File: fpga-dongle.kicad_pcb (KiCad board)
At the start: 2 copper layers, 85.8 x 137 mm, 103 parts, among them P1 USB_PWR, P2 PGM, P3 right, P4 left, P5 CONN_01X40, P6 CONN_01X40, P7 DBG_SWD, P8 USB_PWR, Q1 BC857, SW1 T1107A(6x3,8x2,5MM), U1 W25Q16BVSSIG(SOIC-8_208mil), U2 sc189(Z) 3.3v, U3 sc189(C) 1.2v, U4 iCE40-HX4K-TQ144, U5 AS4C16M16S, U6 LPC11U35FBD48, X1 12MHz

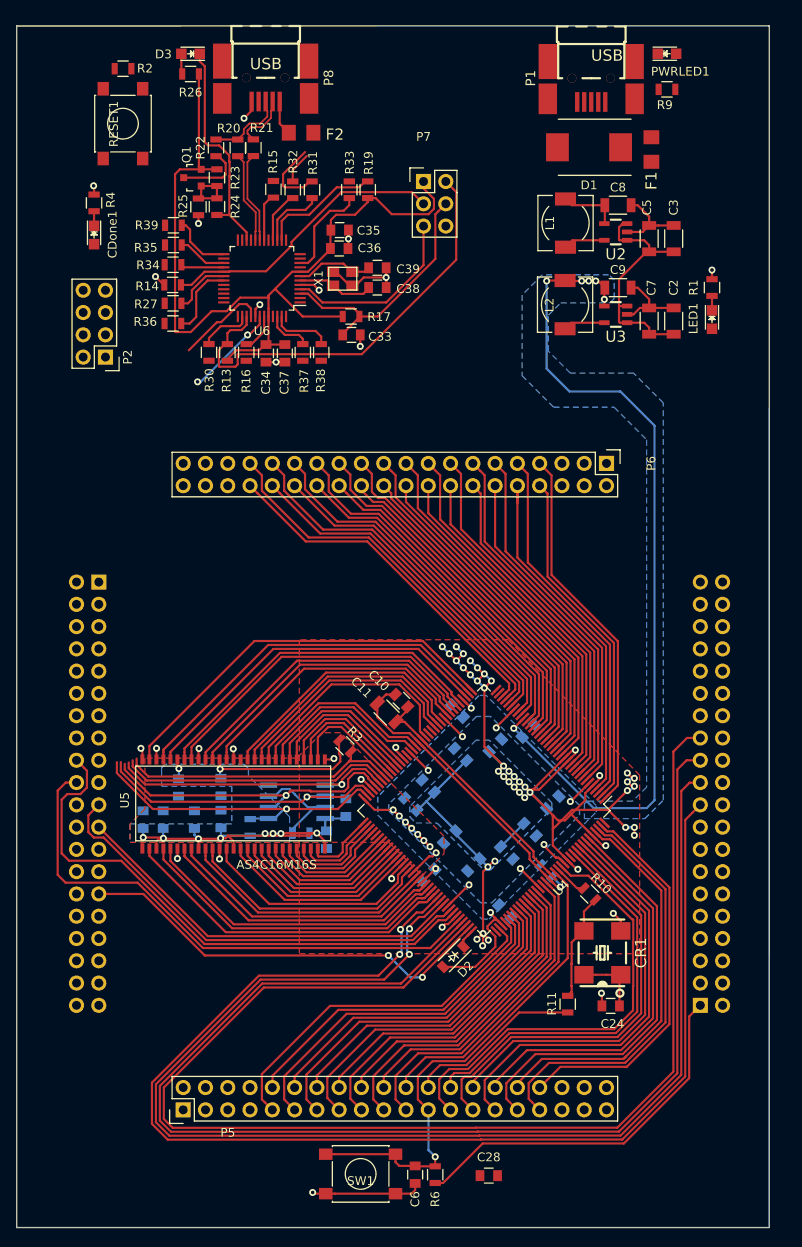
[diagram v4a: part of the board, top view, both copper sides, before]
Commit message: More route (PWR net connectors TODO)
Signed-off-by: Martin Ribelotta <martinribelotta@gmail.com>
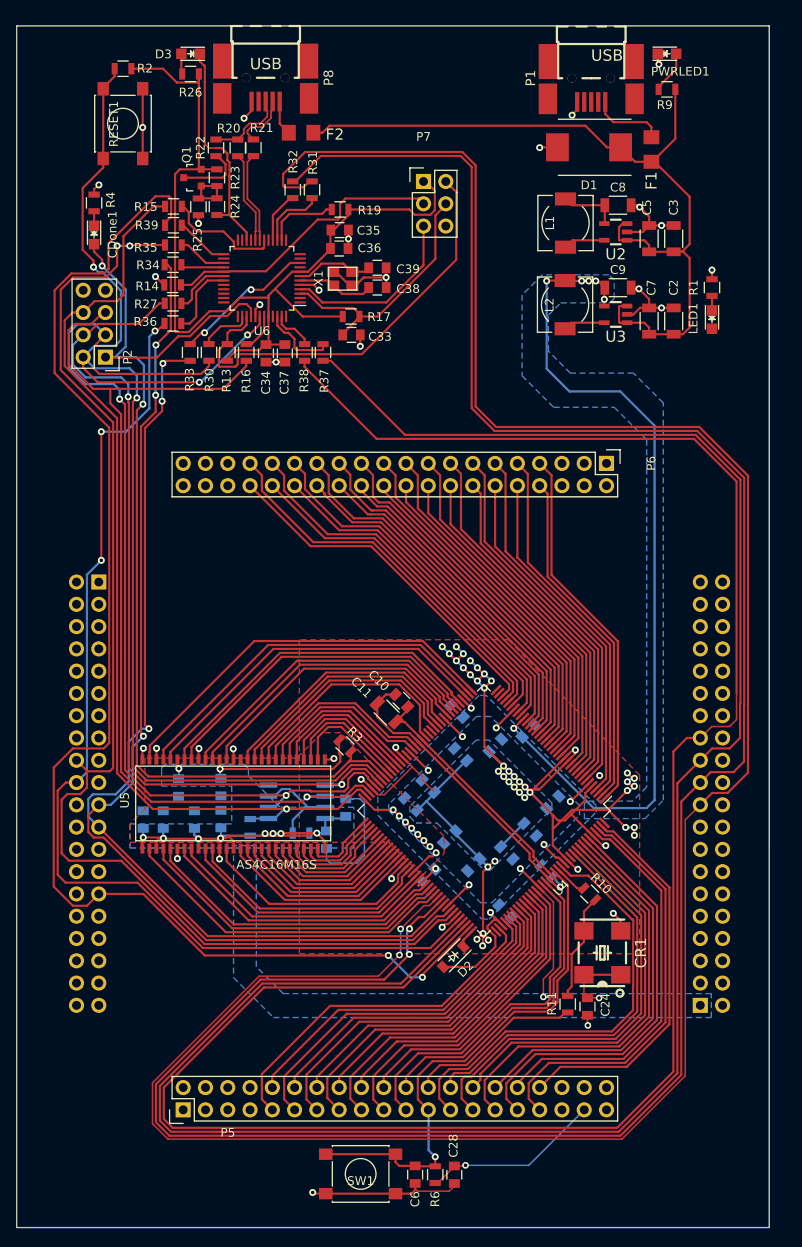
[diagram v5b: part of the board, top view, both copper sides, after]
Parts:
- moved R33 26.0 mm to (35.0, 54.9), turned to 270 degrees
- moved R15 11.6 mm to (33.1, 38.2), turned to 180 degrees
- moved C28 3.93 mm to (65.2, 148.6), turned to 270 degrees
- moved R19 3.87 mm to (52.1, 38.5), turned to 0 degrees
- moved C24 2.65 mm to (80.3, 129.4), turned to 270 degrees
- moved R37 2.30 mm to (50.2, 54.9)
- moved R38 1.90 mm to (48.1, 54.9)
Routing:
- net /I2C_SDA: track 152.7 -> 274.9 mm
- net /I2C_SCL: track 149.5 -> 267.5 mm
- net /iCE40-CRESET: track 41.9 -> 147.5 mm, vias 2 -> 4
- net /GPIO0: track 48.7 -> 153.4 mm
- net /TxD: track 147.0 -> 234.5 mm
- net /RxD: track 146.2 -> 233.5 mm
- net /iCE40-SDI: track 36.2 -> 113.7 mm, vias 1 -> 2
- net /SPI_MISO: track 63.6 -> 139.1 mm, vias 0 -> 2
- net /iCE40-SCK: track 34.1 -> 109.1 mm
- net /iCE40-CDONE: track 42.6 -> 117.3 mm, vias 0 -> 2
- net /iCE40-SS_B: track 37.2 -> 110.8 mm
- net +5V: track 28.4 -> 96.0 mm
- net /SPI_MOSI: track 51.4 -> 117.9 mm, vias 0 -> 3
- net /iCE40-SDO: track 33.6 -> 98.6 mm, vias 1 -> 2
- net /SPI_CS: track 46.0 -> 108.5 mm, vias 0 -> 3
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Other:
- net class Default: clearance 0.2 -> 0.1778; trace_width 0.25 -> 0.1778; via_dia 0.8 -> 0.762; via_drill 0.4 -> 0.4064
- rule trace_clearance: 0.2 -> 0.1778
- rule trace_min: 0.2 -> 0.1778
- rule via_min_drill: 0.3 -> 0.4064
- rule via_min_size: 0.4 -> 0.7112

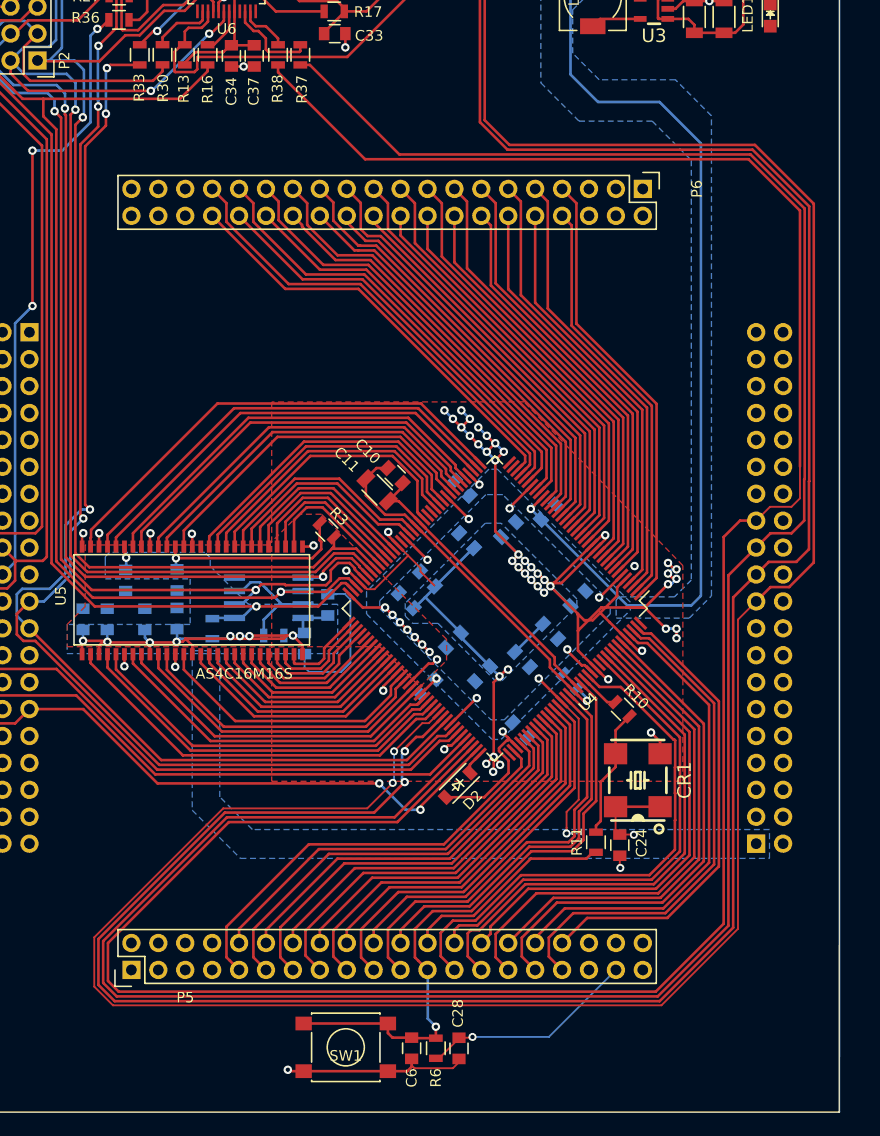
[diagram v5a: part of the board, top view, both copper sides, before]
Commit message: First DRC pass. Remain unconenct some 3v3 and 5v
Signed-off-by: Martin Ribelotta <martinribelotta@gmail.com>
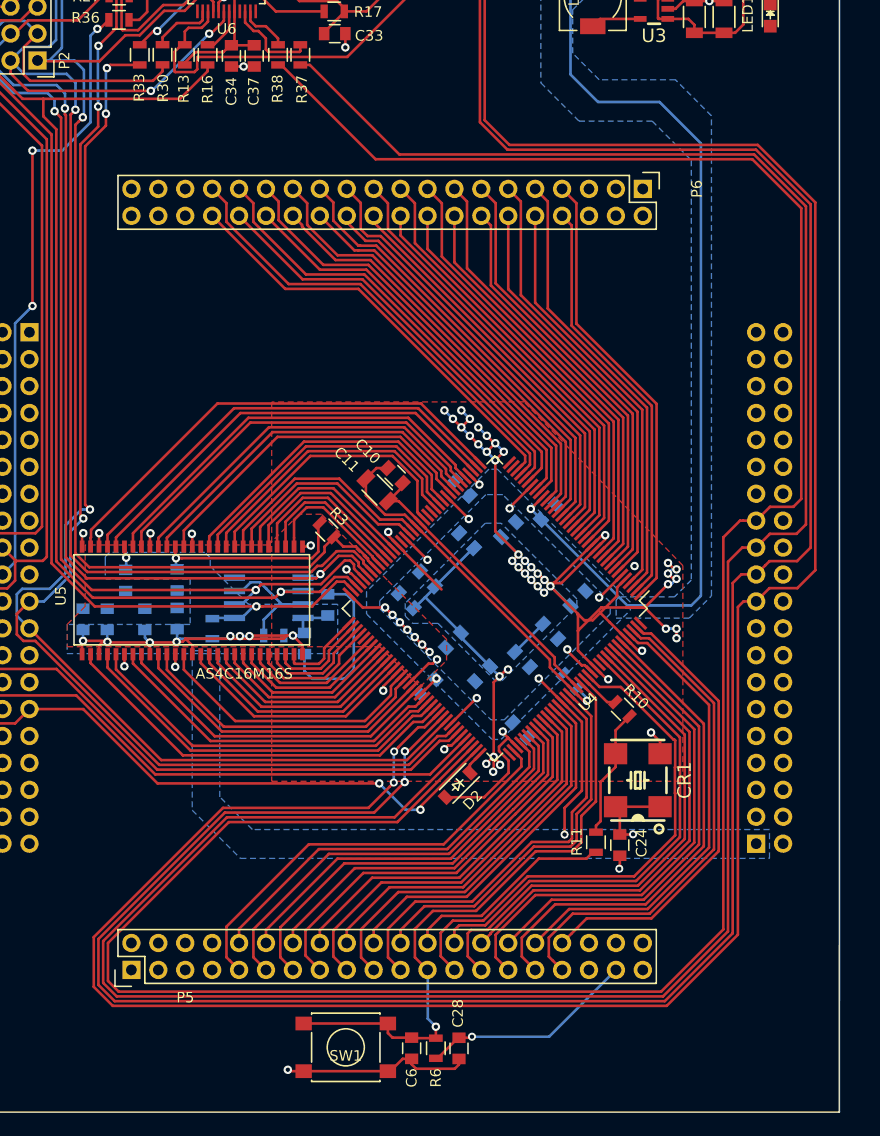
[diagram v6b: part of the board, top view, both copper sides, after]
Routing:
- net GND: track 258.8 -> 254.5 mm
- net /I2C_SDA: track 274.9 -> 276.9 mm
- net /RxD: track 233.5 -> 235.2 mm
- net +3V3: track 263.9 -> 262.6 mm
- net /FPGA_IO_BANK1_17: track 45.6 -> 44.5 mm
- net /FPGA_IO_BANK1_21: track 45.0 -> 43.9 mm
- net /I2C_SCL: track 267.5 -> 268.6 mm
- net /FPGA_IO_BANK1_23: track 44.0 -> 43.2 mm
- net /FPGA_IO_BANK1_22: track 47.7 -> 46.9 mm
- net /FPGA_IO_BANK1_18: track 48.4 -> 47.5 mm
- net /FPGA_IO_BANK1_20: track 47.6 -> 46.8 mm
- net /FPGA_IO_BANK1_19: track 44.6 -> 43.8 mm
- net /FPGA_IO_BANK1_16: track 49.2 -> 48.4 mm
- net /FPGA_IO_BANK1_15: track 46.6 -> 45.8 mm
- net /FPGA_IO_BANK1_14: track 50.5 -> 49.7 mm
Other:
- net class Default: clearance 0.1778 -> 0.1905; trace_width 0.1778 -> 0.25
- rule trace_clearance: 0.1778 -> 0.1905
- rule trace_min: 0.1778 -> 0.2032

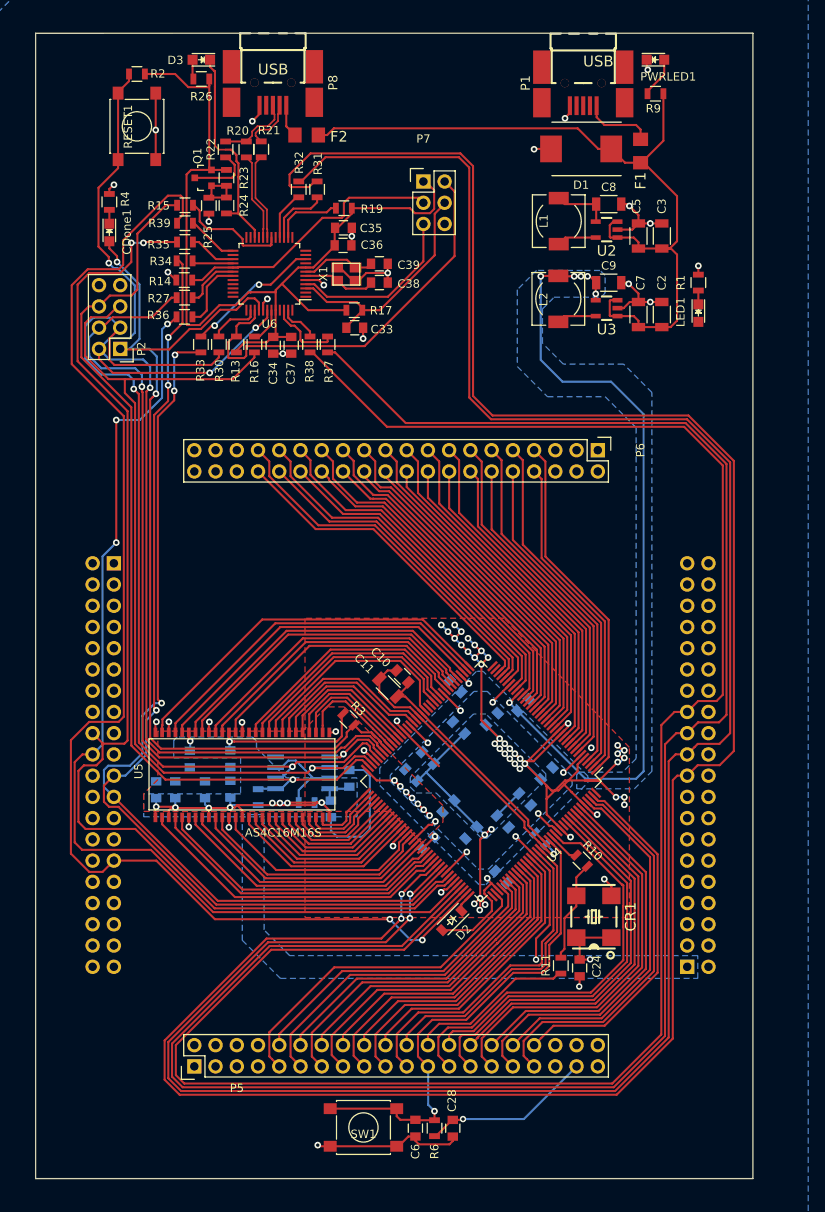
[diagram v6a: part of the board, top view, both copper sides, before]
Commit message: Fix CIAA connector side error, power net route
Signed-off-by: Martin Ribelotta <martinribelotta@gmail.com>
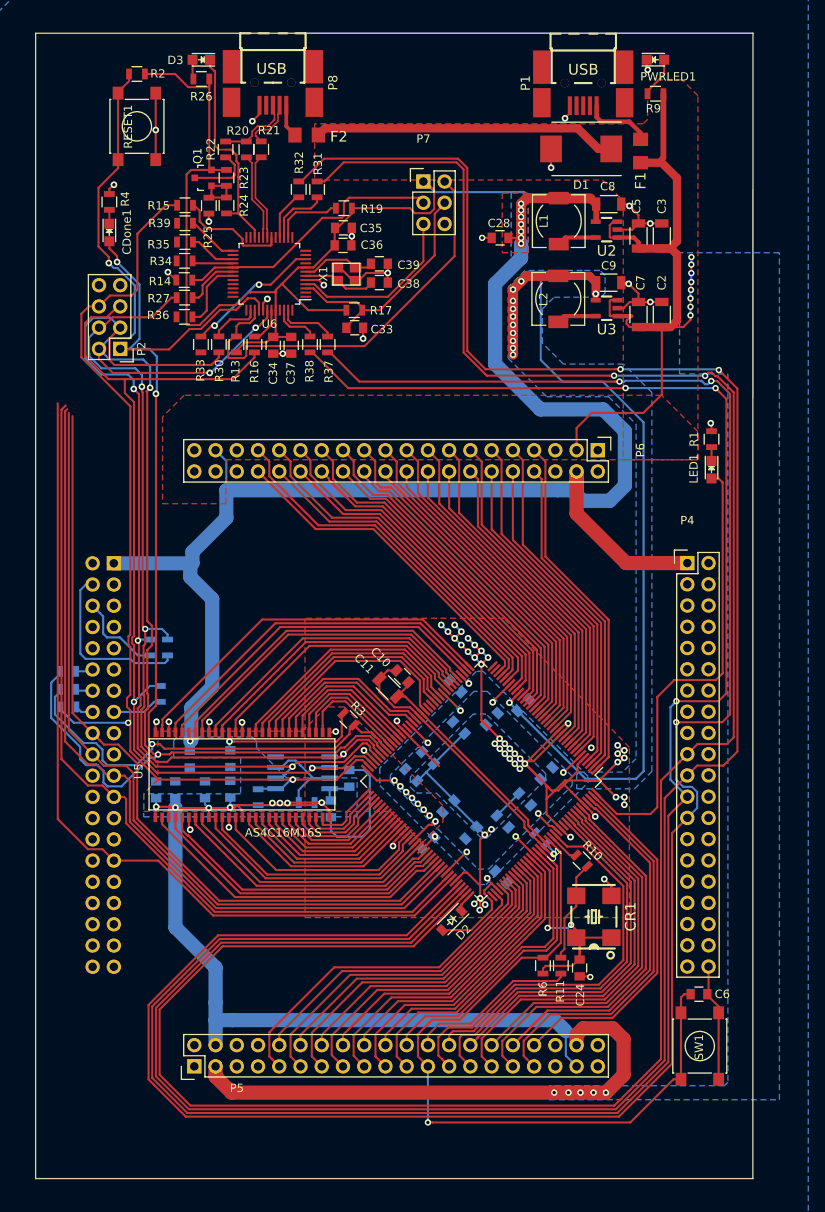
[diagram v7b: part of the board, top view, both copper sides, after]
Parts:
- added R18: 100R, Resistors_SMD:R_0805, B.Cu at (28.9, 91.1)
- added R28: 100R, Resistors_SMD:R_0805, B.Cu at (19.2, 98.2)
- added R29: 100R, Resistors_SMD:R_0805, B.Cu at (30.2, 96.7)
- added R40: 100R, Resistors_SMD:R_0805, B.Cu at (19.1, 96.1)
- added R41: 100R, Resistors_SMD:R_0805, B.Cu at (19.1, 94.0)
- added R7: 100R, Resistors_SMD:R_0805, B.Cu at (31.1, 91.1)
- P4: moved to F.Cu
- moved C28 106.7 mm to (70.8, 42.1), turned to 180 degrees
- moved P4 48.3 mm to (93.2, 81.0)
- moved SW1 41.4 mm to (94.7, 138.8), turned to 270 degrees
- moved C6 37.5 mm to (94.6, 132.6), turned to 180 degrees
- moved R6 23.4 mm to (76.0, 129.2)
- moved LED1 18.8 mm to (96.1, 69.8)
- moved R1 18.8 mm to (96.1, 66.2)
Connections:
- P3 pad 12: (no net) -> /AUX_CRESET
- P3 pad 14: (no net) -> /AUX_CDONE
- P3 pad 15: (no net) -> /AUX_SPI_SCK
- P3 pad 16: (no net) -> /AUX_SPI_SSEL
- P3 pad 4: (no net) -> /AUX_SPI_MISO
- P3 pad 6: (no net) -> /AUX_SPI_MOSI
- P4 pad 10: GNDA -> GND
- P4 pad 12: GNDA -> GND
- P4 pad 14: GNDA -> GND
- P4 pad 16: GNDA -> GND
- P4 pad 18: GNDA -> GND
- P4 pad 8: GNDA -> GND
- R37 pad 1: /P_RxD -> /P_TxD
- R37 pad 2: /RxD -> /TxD
- R38 pad 1: /P_TxD -> /P_RxD
- R38 pad 2: /TxD -> /RxD
- U4 pad 101: /SPI_MOSI -> /SPI_CS
- U4 pad 102: /SPI_MISO -> /GPIO0
- U4 pad 104: /SPI_CLK -> /TxD
- U4 pad 106: /TxD -> /I2C_SCL
- U4 pad 107: /GPIO0 -> /I2C_SDA
- U4 pad 97: /I2C_SDA -> /SPI_MISO
- U4 pad 98: /I2C_SCL -> /SPI_CLK
- U4 pad 99: /SPI_CS -> /SPI_MOSI
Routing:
- net +3V3: track 262.6 -> 519.4 mm, vias 28 -> 34
- net +5V: track 96.0 -> 191.8 mm, vias 0 -> 13
- net /LED1: track 0.00 -> 55.3 mm
- net /GPIO0: track 153.4 -> 103.5 mm, vias 2 -> 0
- net /SPI_MISO: track 139.1 -> 94.1 mm, vias 2 -> 0
- net /BUT1: track 60.0 -> 89.1 mm
- net /iCE40-CRESET: track 147.8 -> 174.9 mm, vias 4 -> 5
- net /SPI_CLK: track 121.0 -> 96.2 mm, vias 3 -> 0
- net /TxD: track 234.8 -> 258.5 mm, vias 0 -> 3
- net /RxD: track 235.2 -> 256.2 mm, vias 0 -> 3
- net /AUX_SPI_MISO: track 0.00 -> 21.0 mm
- net /iCE40-CDONE: track 117.4 -> 137.4 mm, vias 2 -> 3
- net /SPI_MOSI: track 117.9 -> 98.1 mm, vias 3 -> 0
- net /I2C_SCL: track 268.6 -> 279.3 mm
- net /AUX_SPI_MOSI: track 0.00 -> 10.5 mm
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- added copper zone on B.Cu, net +5V
- added copper zone on F.Cu, net +5V

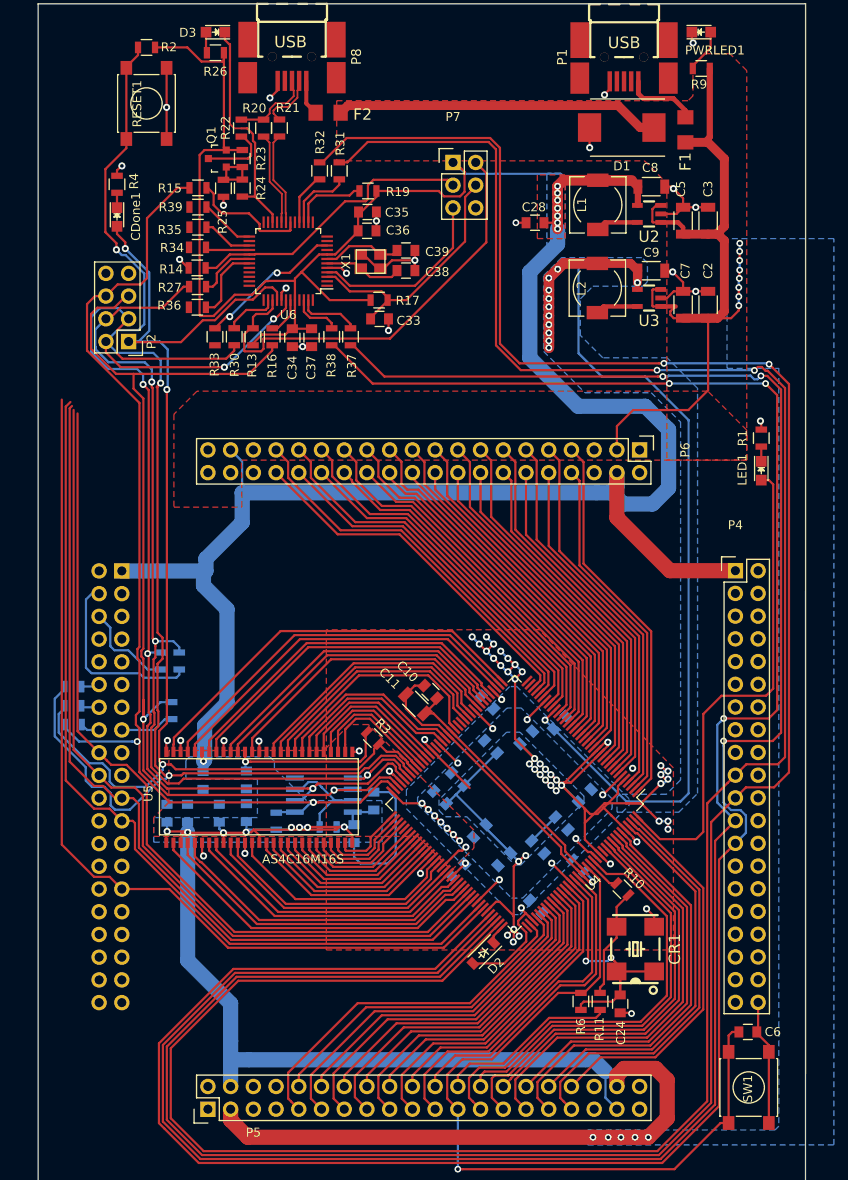
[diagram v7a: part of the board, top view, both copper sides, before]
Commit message: Fix CIAA connector side. Reroute bad lines. First DRC of PCB
Signed-off-by: Martin Ribelotta <martinribelotta@gmail.com>
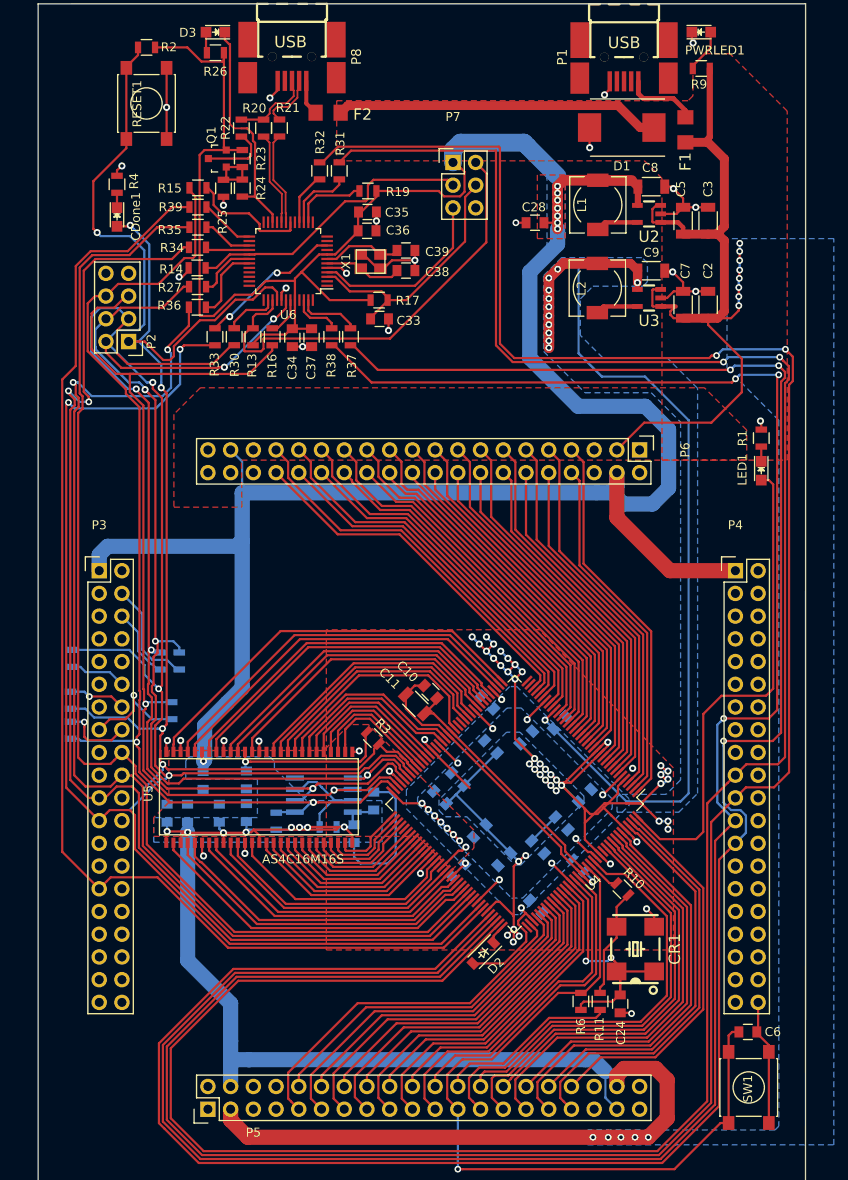
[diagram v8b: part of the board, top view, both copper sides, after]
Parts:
- P3: moved to F.Cu
- moved R41 3.15 mm to (19.1, 90.8), turned to 90 degrees
- moved P3 2.53 mm to (22.1, 81.0), turned to 0 degrees
- moved R28 0.69 mm to (18.9, 98.8), turned to 270 degrees
- moved R40 0.67 mm to (18.9, 95.5), turned to 270 degrees
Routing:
- net /SPI_MOSI: track 98.1 -> 133.5 mm, vias 0 -> 2
- net /SPI_MISO: track 94.1 -> 128.1 mm
- net /GPIO0: track 103.5 -> 136.0 mm
- net /SPI_CLK: track 96.2 -> 125.0 mm, vias 0 -> 2
- net /SPI_CS: track 99.9 -> 123.5 mm, vias 0 -> 2
- net +3V3: track 519.4 -> 528.2 mm
- net /AUX_SPI_MISO: track 21.0 -> 12.3 mm
- net /iCE40-CRESET: track 174.9 -> 168.1 mm, vias 5 -> 6
- net /AUX_SPI_SCK: track 6.06 -> 12.2 mm, vias 0 -> 1
- net /AUX_SPI_SSEL: track 2.20 -> 8.07 mm, vias 0 -> 1
- net /AUX_CDONE: track 2.07 -> 6.60 mm, vias 0 -> 1
- net /AUX_CRESET: track 2.09 -> 6.36 mm
- net +5V: track 191.8 -> 195.7 mm
- net /iCE40-SCK: track 116.0 -> 113.4 mm
- net /AUX_SPI_MOSI: track 10.5 -> 8.00 mm
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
